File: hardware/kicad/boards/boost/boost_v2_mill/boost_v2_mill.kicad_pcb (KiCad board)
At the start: 2 copper layers, 116.2 x 97.3 mm, 17 parts, among them J1 lager ind (5V), J2 V2 ud (10V), J3 PWM (isoleret), J4 drive +15V, M1 IRF530, U1 CNY17, U2 IR2110

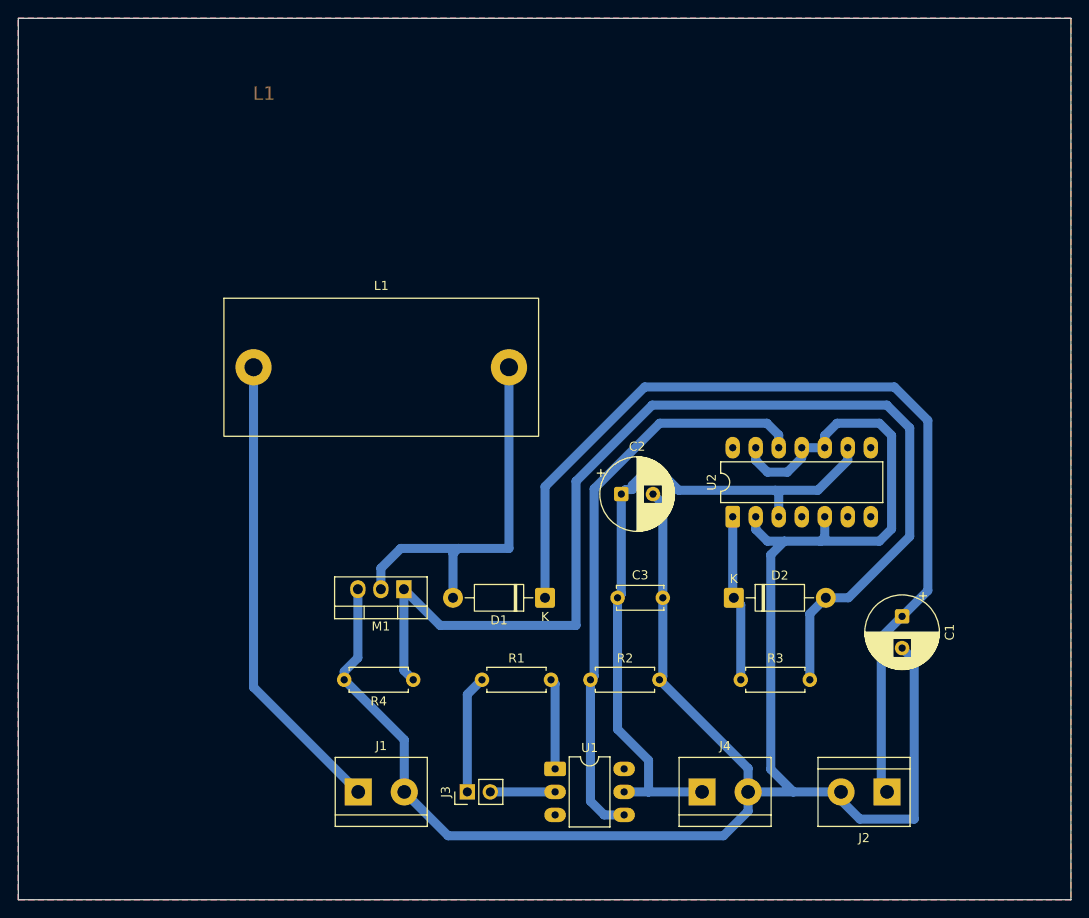
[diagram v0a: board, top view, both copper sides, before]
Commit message: boost_v2_mill: fillet Edge.Cuts corners, regenerate cutout at 2.3 mm
Rounded the four board corners (Edge.Cuts now 4 lines + 4 arcs) and
re-exported the Edge.Cuts gerber. Regenerated the cutout toolpath (.nc
and .rml) from the new outline at 2.3 mm full-breakthrough depth, matching
the drilled holes. Traces and drill toolpaths are unchanged (no copper
near the rounded corners). Bumps the srm-cam pointer to the 2.3 mm preset.
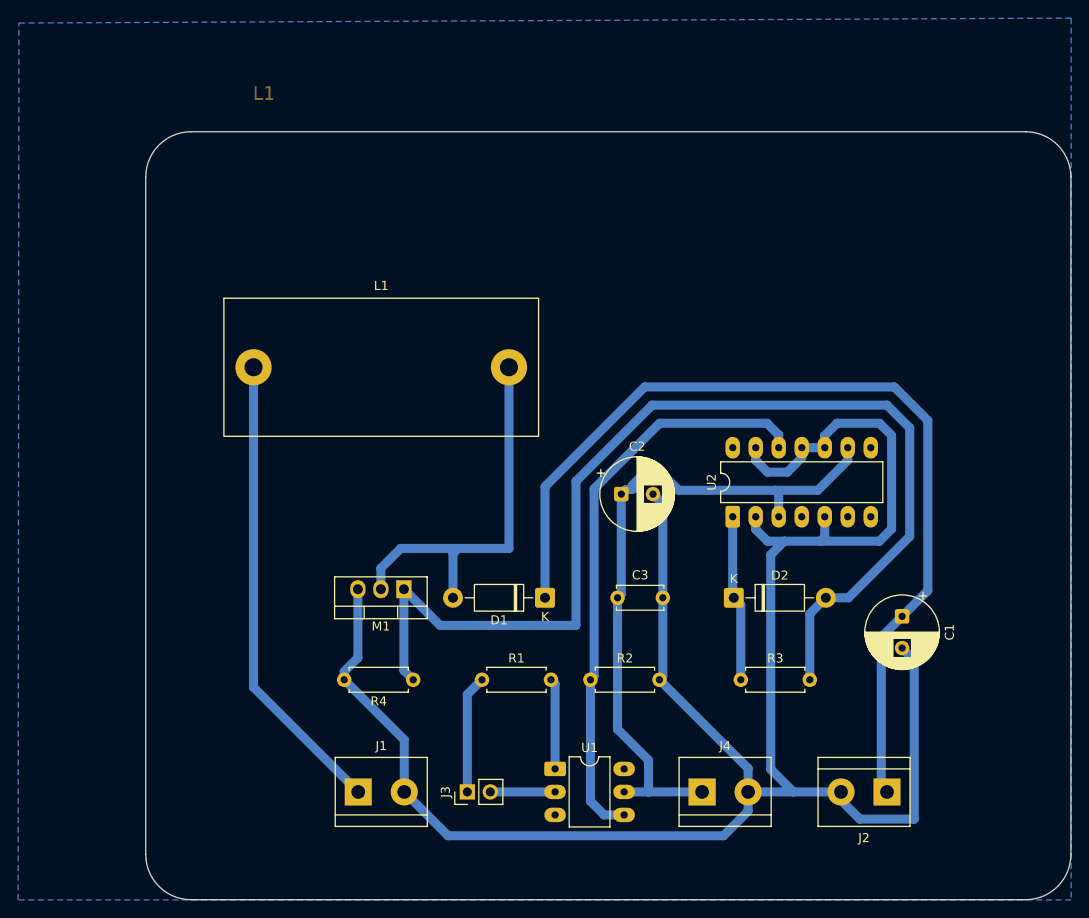
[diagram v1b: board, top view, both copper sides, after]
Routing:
- removed copper zone on F.Cu, net (none)
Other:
- board size 116.2 x 97.3 mm -> 102.1 x 84.8 mm
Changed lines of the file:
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@@
 		(tenting front back)
 		(pcbplotparams
-			(layerselection 0x00000000_00000000_55555555_5755f5ff)
+			(layerselection 0x00000000_00000000_55555555_57555554)
 			(plot_on_all_layers_selection 0x00000000_00000000_00000000_00000000)
 			(disableapertmacros no)
-			(usegerberextensions no)
+			(usegerberextensions yes)
 			(usegerberattributes yes)
 			(usegerberadvancedattributes yes)
@@
 			(outputformat 1)
 			(mirror no)
-			(drillshape 1)
+			(drillshape 0)
 			(scaleselection 1)
-			(outputdirectory "")
+			(outputdirectory "../../../production/boost_v2/gerbers/")
 		)
 	)
@@
 		)
 	)
-	(gr_rect
-		(start 17.435882 36.981004)
-		(end 133.635882 134.281004)
+	(gr_line
+		(start 128.635882 134.281004)
+		(end 36.5 134.281004)
+		(stroke
+			(width 0.05)
+			(type default)
+		)
+		(layer "Edge.Cuts")
+	)
+	(gr_arc
+		(start 128.635882 49.5)
+		(mid 132.171416 50.964466)
+		(end 133.635882 54.5)
+		(stroke
+			(width 0.05)
+			(type default)
+		)
+		(layer "Edge.Cuts")
+	)
+	(gr_line
+		(start 36.5 49.5)
+		(end 128.635882 49.5)
+		(stroke
+			(width 0.05)
+			(type default)
+		)
+		(layer "Edge.Cuts")
+	)
+	(gr_arc
+		(start 133.635882 129.281004)
+		(mid 132.171413 132.816529)
+		(end 128.635882 134.281004)
+		(stroke
+			(width 0.05)
+			(type default)
+		)
+		(layer "Edge.Cuts")
+	)
+	(gr_arc
+		(start 31.5 54.5)
+		(mid 32.964466 50.964466)
+		(end 36.5 49.5)
+		(stroke
+			(width 0.05)
+			(type default)
+		)
+		(layer "Edge.Cuts")
+	)
+	(gr_line
+		(start 133.635882 54.5)
+		(end 133.635882 129.281004)
+		(stroke
+			(width 0.05)
+			(type default)
+		)
+		(layer "Edge.Cuts")
+	)
+	(gr_line
+		(start 31.5 129.281004)
+		(end 31.5 54.5)
+		(stroke
+			(width 0.05)
+			(type default)
+		)
+		(layer "Edge.Cuts")
+	)
+	(gr_arc
+		(start 36.5 134.281004)
+		(mid 32.964465 132.816538)
+		(end 31.5 129.281004)
 		(stroke
 			(width 0.05)
 			(type default)
 		)
-		(fill no)
 		(layer "Edge.Cuts")
 	)
@@
 		(net 0)
 		(net_name "")
-		(layer "F.Cu")
-		(hatch edge 0.5)
-		(connect_pads no
-			(clearance 1.2)
-		)
-		(min_thickness 0.25)
-		(filled_areas_thickness no)
-		(fill yes
-			(thermal_gap 0.5)
-			(thermal_bridge_width 0.5)
-		)
-		(polygon
-			(pts
-				(xy 17.410882 36.956004) (xy 133.660882 36.956004) (xy 133.660882 134.306004) (xy 17.410882 134.306004)
-			)
-		)
-	)
-	(zone
-		(net 0)
-		(net_name "")
 		(layer "B.Cu")
 		(hatch edge 0.5)
@@
 		(polygon
 			(pts
-				(xy 17.410882 36.956004) (xy 133.660882 36.956004) (xy 133.660882 134.306004) (xy 17.410882 134.306004)
+				(xy 17.5 37.5) (xy 133.660882 36.956004) (xy 133.660882 134.306004) (xy 17.410882 134.306004)
 			)
 		)
